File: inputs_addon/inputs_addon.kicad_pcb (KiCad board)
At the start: 2 copper layers, 50 x 50 mm, 19 parts, among them J1 Conn_01x14_Female, J2 Conn_01x14_Male, SW1 SW_Push, SW2 SW_Push

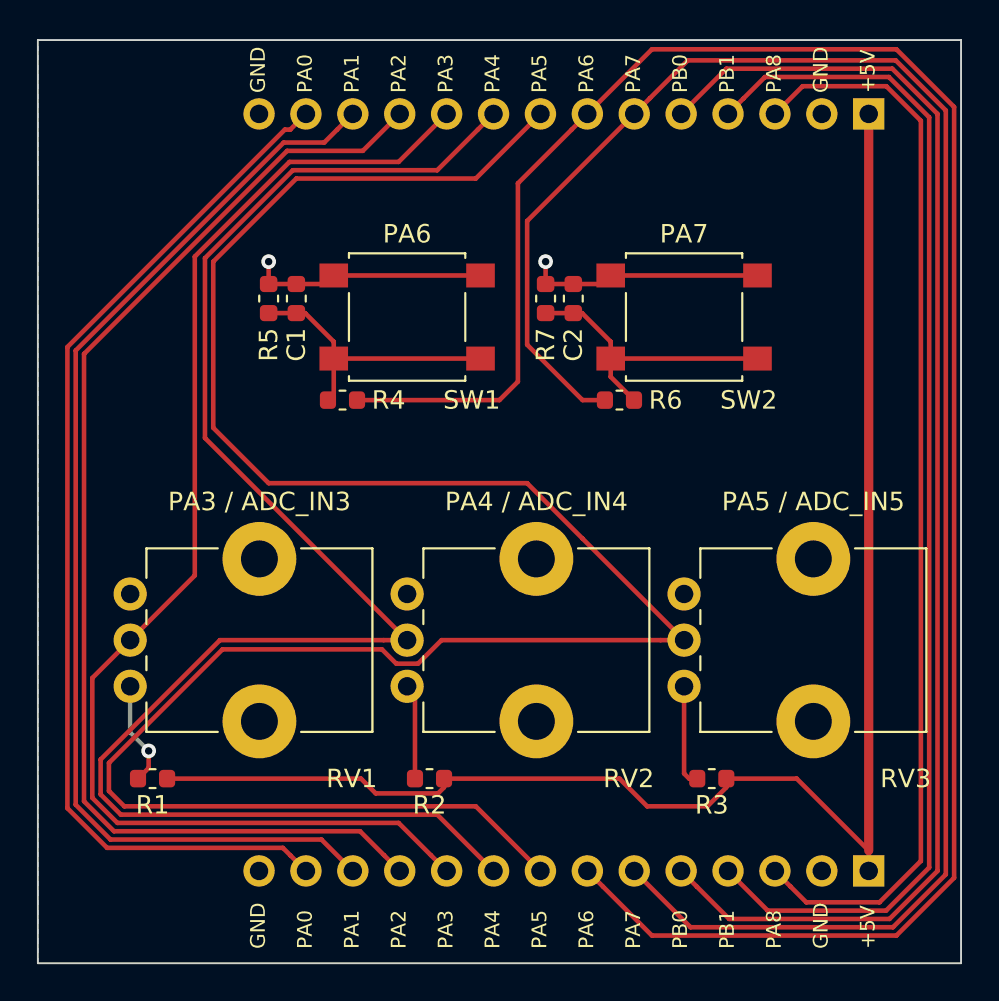
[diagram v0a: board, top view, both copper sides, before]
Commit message: switch to vertical headers, add mounting holes
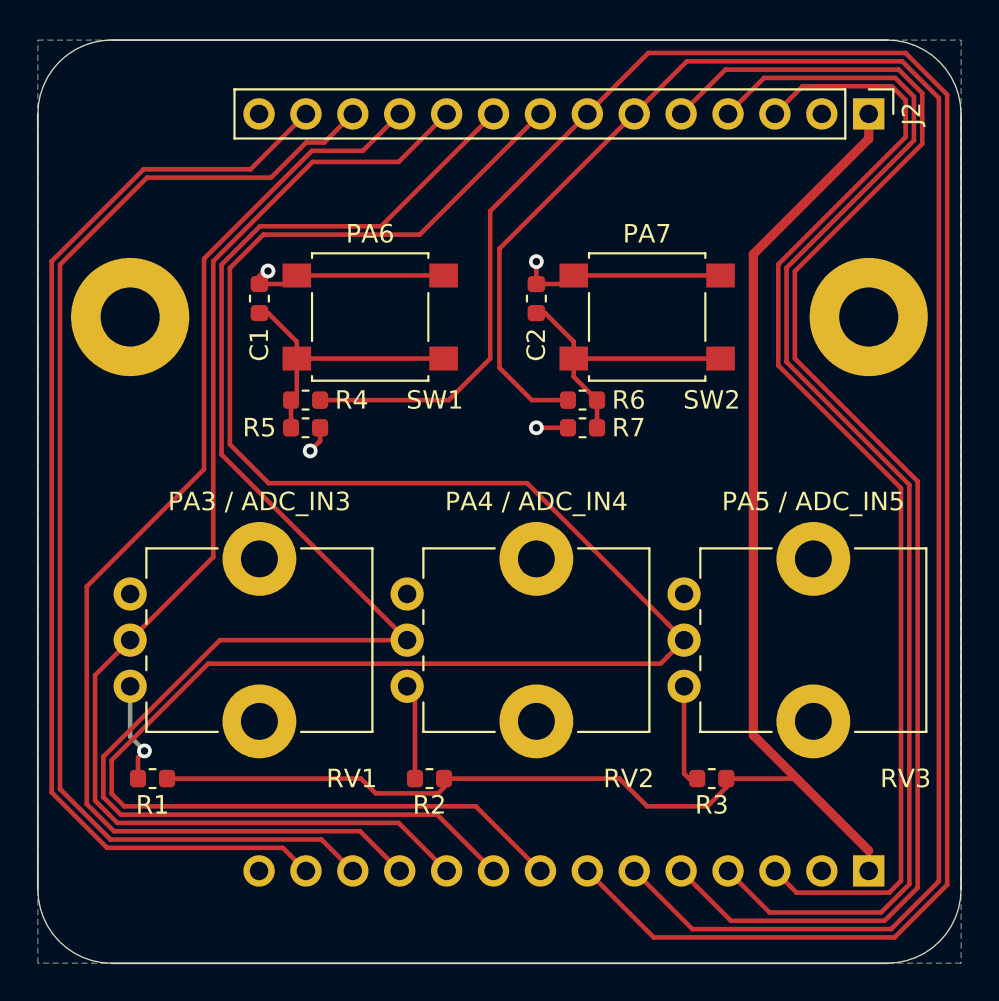
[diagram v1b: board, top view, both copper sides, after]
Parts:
- added H1: MountingHole_Pad, MountingHole:MountingHole_3.2mm_M3_Pad, F.Cu at (155.0, 115.0)
- added H2: MountingHole_Pad, MountingHole:MountingHole_3.2mm_M3_Pad, F.Cu at (195.0, 115.0)
- J1: footprint Connector_PinSocket_2.54mm:PinSocket_1x14_P2.54mm_Horizontal -> Connector_PinSocket_2.54mm:PinSocket_1x14_P2.54mm_Vertical
- J2: footprint Connector_PinHeader_2.54mm:PinHeader_1x14_P2.54mm_Horizontal -> Connector_PinHeader_2.54mm:PinHeader_1x14_P2.54mm_Vertical; moved to F.Cu
- moved R5 7.28 mm to (164.5, 121.0), turned to 0 degrees
- moved R7 7.28 mm to (179.5, 121.0), turned to 180 degrees
- moved C1 2.00 mm to (162.0, 114.0)
- moved C2 2.00 mm to (177.0, 114.0)
- moved R4 2.00 mm to (164.5, 119.5)
- moved R6 2.00 mm to (179.5, 119.5)
- moved SW1 2.00 mm to (168.0, 115.0)
- moved SW2 2.00 mm to (183.0, 115.0)
- turned J2 to 270 degrees
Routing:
- net +5V: track 83.1 -> 88.3 mm
- net /PB0: track 73.0 -> 77.9 mm
- net /PB1: track 66.0 -> 71.0 mm
- net /PA8: track 58.9 -> 63.5 mm
- net /PA1: track 61.4 -> 65.3 mm
- net /PA0: track 57.5 -> 61.4 mm
- net /PA5: track 121.5 -> 119.3 mm
- net /PA4: track 88.3 -> 86.7 mm
- net /PA2: track 65.4 -> 64.5 mm
- net /PA3: track 69.3 -> 68.4 mm
- net /PA7: track 100.3 -> 101.0 mm
- net GND: track 25.8 -> 25.7 mm, vias 2 -> 4
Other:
- outline, holes or cut-outs redrawn
